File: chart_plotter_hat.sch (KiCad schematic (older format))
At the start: 41 parts, among them J1 Conn_01x06, J2 Conn_01x04, J3 40HAT, J4 Conn_01x04, J5 Conn_01x04, J6 Conn_01x02, J7 Conn_01x04, J8 Conn_02x03_Odd_Even, J9 Conn_01x03, Q1 DMG2305UX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

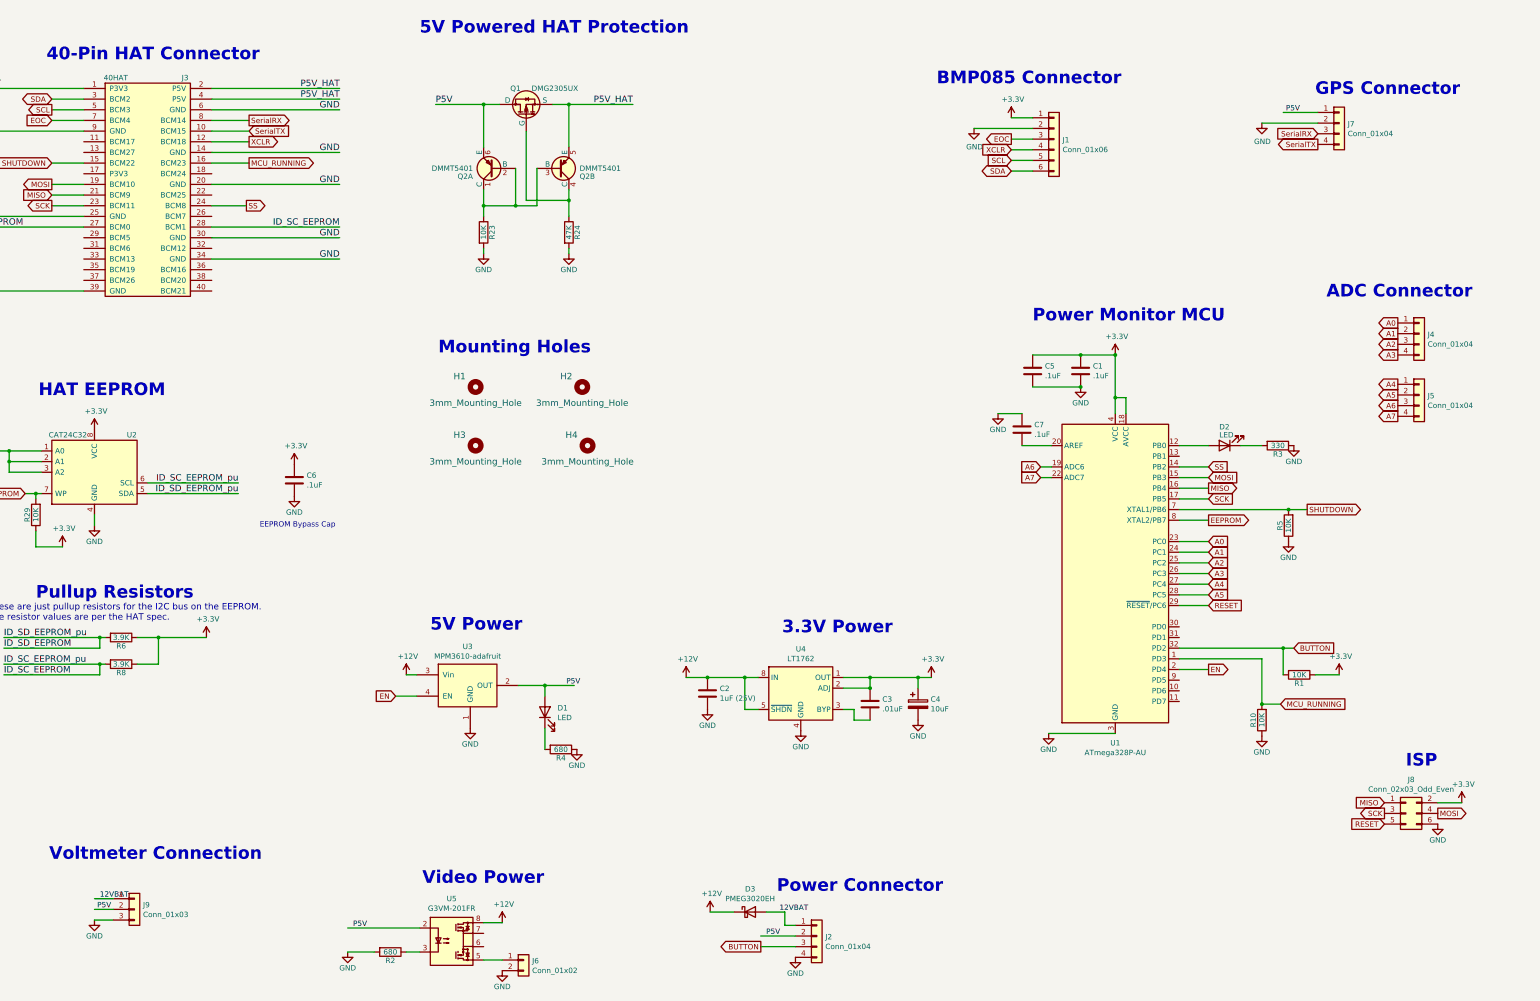
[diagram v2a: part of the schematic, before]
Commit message: Added Inductor to AVCC
Added optional 12VBAT adc on A7
Changed P5V label to +5V
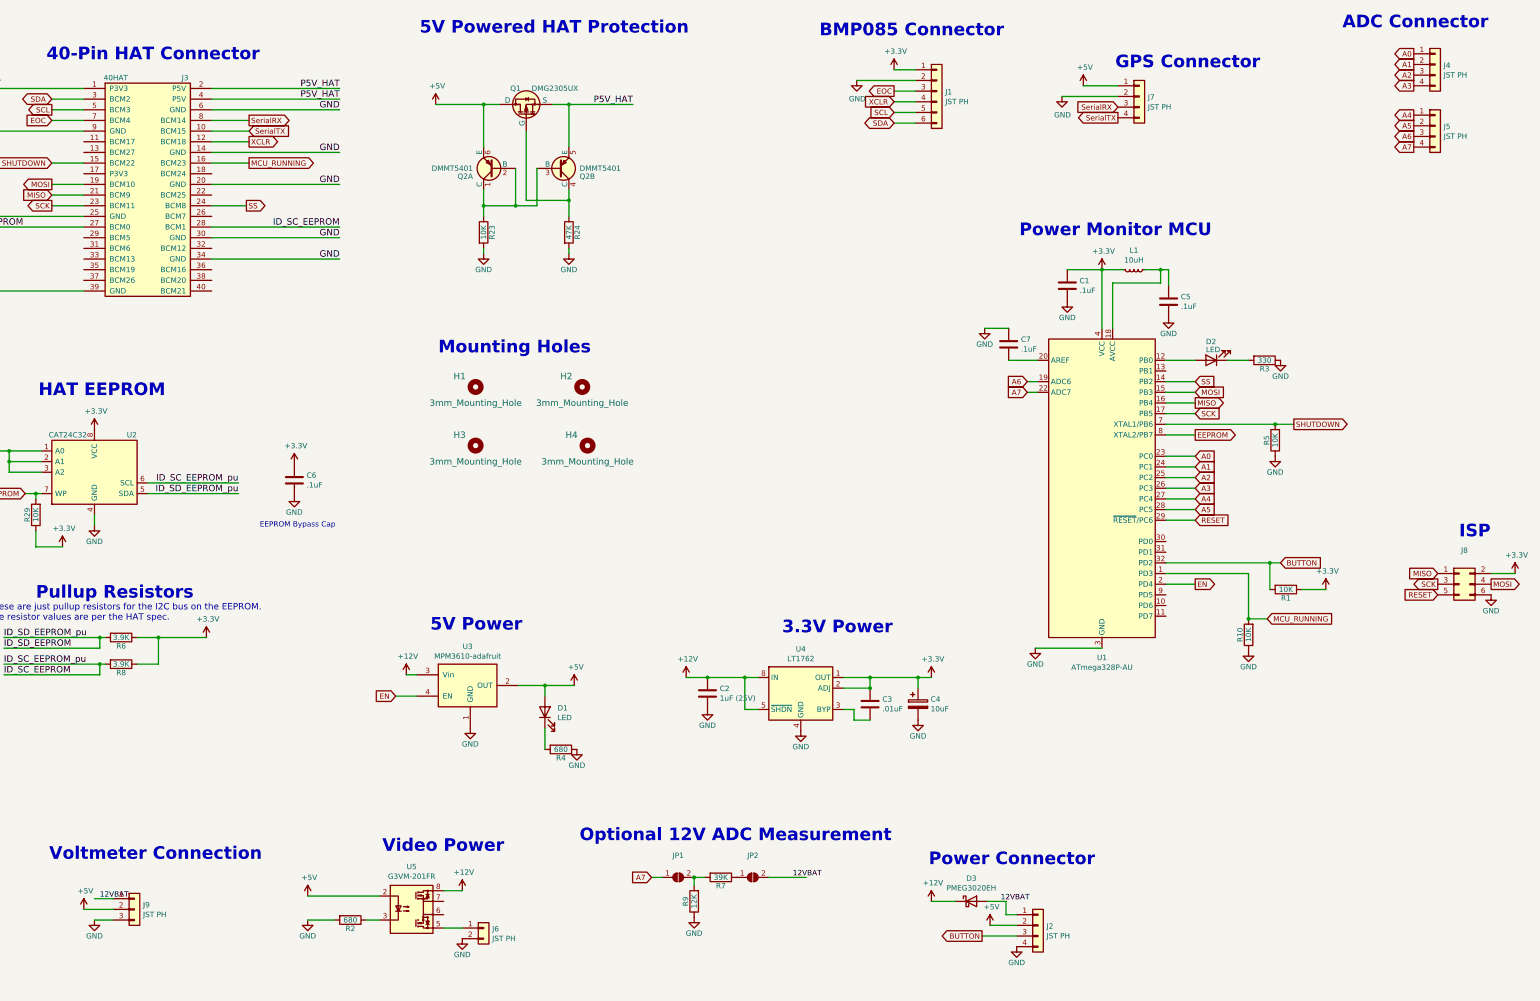
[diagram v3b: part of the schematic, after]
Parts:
- added JP1, JP2: SolderJumper_2_Open, CustomComponents:SolderJumper-2_P1.3mm_Open_RoundedPad1.0x1.5mm, symbol Jumper:SolderJumper_2_Open
- added L1: 10uH, Capacitors_SMD:C_0603, symbol Device:L_Small
- added R7: 39K, Resistors_SMD:R_0603, symbol Device:R
- added R9: 12K, Resistors_SMD:R_0603, symbol Device:R
- J1: value Conn_01x06 -> JST PH
- J2, J4, J5, J7: value Conn_01x04 -> JST PH
- J6: value Conn_01x02 -> JST PH
- J9: value Conn_01x03 -> JST PH
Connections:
- net labels added: +5V
- net labels removed: P5V
- wire segments 149 -> 155
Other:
- note added: "Optional 12V ADC Measurement"
- moved on the sheet: C1, C5, C7, D2, D3, J1, J2, J4, J5, J6, J7, J8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

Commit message: Added pdf of original release
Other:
- note added: "To use, solder both bridges, and populate R7 and R9"
- moved on the sheet: C1, C2, C3, C4, C5, C6, C7, D1, D2, D3, J2, J6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

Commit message: Moved CS to PD3, MCU_RUNNING to PB1
Renamed SS to CS
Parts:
- C2: value 1uF (25V) -> 1uF; Voltage (none) -> 25V
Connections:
- net MCU_RUNNING: now also U1.13 (PB1); no longer U1.1 (PD3)
- net SS: no longer names the net of U1.14 (PB2)
- net SS: no longer J3.24 (BCM8)
- new net CS: J3.24 (BCM8), U1.1 (PD3)
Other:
- moved on the sheet: R10
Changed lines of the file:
@@
 Wire Wire Line
 	13100 5925 13375 5925
-Text GLabel 13375 5625 2    50   Input ~ 0
-SS
-Wire Wire Line
-	13100 5625 13375 5625
+Text GLabel 13375 7425 2    50   Input ~ 0
+CS
+Wire Wire Line
+	13100 5525 14950 5525
 Wire Wire Line
 	13100 7525 13375 7525
@@
 	2000 3350 1700 3350
 Text GLabel 3525 3350 2    50   Output ~ 0
-SS
+CS
 Wire Wire Line
 	3200 3350 3525 3350
@@
 Text GLabel 14300 6025 2    50   Output ~ 0
 SHUTDOWN
-Text GLabel 14050 7850 2    50   Input ~ 0
+Text GLabel 15125 5950 2    50   Input ~ 0
 MCU_RUNNING
 Text GLabel 14175 7325 2    50   Input ~ 0
@@
 L power:GND #PWR015
 U 1 1 5FDCD1F3
-P 13875 8150
-F 0 "#PWR015" H 13875 7900 50  0001 C CNN
-F 1 "GND" H 13875 8000 50  0000 C CNN
-F 2 "" H 13875 8150 50  0000 C CNN
-F 3 "" H 13875 8150 50  0000 C CNN
-	1    13875 8150
+P 14950 6250
+F 0 "#PWR015" H 14950 6000 50  0001 C CNN
+F 1 "GND" H 14950 6100 50  0000 C CNN
+F 2 "" H 14950 6250 50  0000 C CNN
+F 3 "" H 14950 6250 50  0000 C CNN
+	1    14950 6250
 	1    0    0    -1
 $EndComp
@@
 P 7850 7525
 F 0 "C2" H 7965 7571 50  0000 L CNN
-F 1 "1uF (25V)" H 7965 7480 50  0000 L CNN
+F 1 "1uF" H 7965 7480 50  0000 L CNN
 F 2 "Capacitors_SMD:C_1206" H 7888 7375 50  0001 C CNN
 F 3 "~" H 7850 7525 50  0001 C CNN
+F 4 "25V" H 8025 7400 50  0000 C CNN "Voltage"
 	1    7850 7525
 	1    0    0    -1
@@
 	3200 2950 3550 2950
 Wire Wire Line
-	13875 7425 13875 7850
-Wire Wire Line
-	13875 7850 14050 7850
-Wire Wire Line
-	13100 7425 13875 7425
+	14950 5525 14950 5950
+Wire Wire Line
+	14950 5950 15125 5950
 $Comp
 L Device:R R10
 U 1 1 5FF805D9
-P 13875 8000
-F 0 "R10" V 13955 8000 50  0000 C CNN
-F 1 "10K" V 13875 8000 50  0000 C CNN
-F 2 "Resistors_SMD:R_0603" V 13805 8000 50  0001 C CNN
-F 3 "" H 13875 8000 50  0001 C CNN
-	1    13875 8000
+P 14950 6100
+F 0 "R10" V 15030 6100 50  0000 C CNN
+F 1 "10K" V 14950 6100 50  0000 C CNN
+F 2 "Resistors_SMD:R_0603" V 14880 6100 50  0001 C CNN
+F 3 "" H 14950 6100 50  0001 C CNN
+	1    14950 6100
 	-1   0    0    1
 $EndComp
-Connection ~ 13875 7850
+Connection ~ 14950 5950
 $Comp
 L power:GND #PWR0111
@@
 Text Notes 6575 9450 0    50   ~ 0
 To use, solder both bridges, and populate R7 and R9
+Wire Wire Line
+	13100 7425 13375 7425
 $EndSCHEMATC

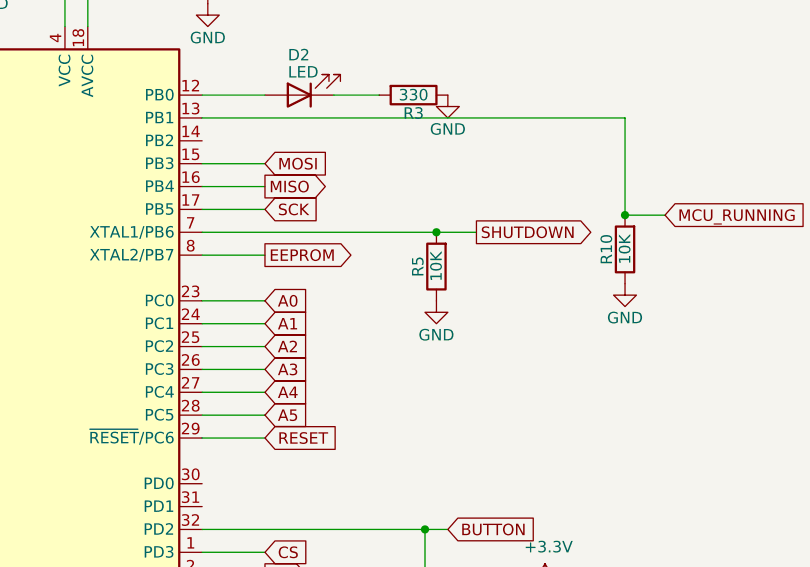
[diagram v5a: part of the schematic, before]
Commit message: Removed pull down on SHUTDOWN, not needed
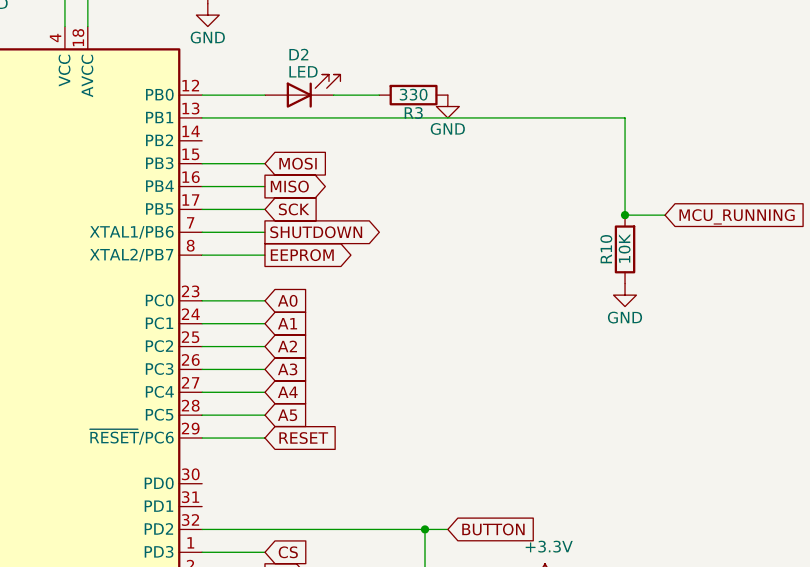
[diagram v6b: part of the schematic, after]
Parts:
- removed R5: 10K, Resistors_SMD:R_0603, symbol Device:R
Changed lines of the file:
@@
 	1    0    0    -1
 $EndComp
-Text GLabel 14300 6025 2    50   Output ~ 0
+Text GLabel 13375 6025 2    50   Output ~ 0
 SHUTDOWN
 Text GLabel 15125 5950 2    50   Input ~ 0
@@
 	13675 5425 13875 5425
 $Comp
-L Device:R R5
-U 1 1 6013CE2D
-P 14125 6175
-F 0 "R5" V 14205 6175 50  0000 C CNN
-F 1 "10K" V 14125 6175 50  0000 C CNN
-F 2 "Resistors_SMD:R_0603" V 14055 6175 50  0001 C CNN
-F 3 "" H 14125 6175 50  0001 C CNN
-	1    14125 6175
-	-1   0    0    1
-$EndComp
-Wire Wire Line
-	13100 6025 14125 6025
-Connection ~ 14125 6025
-Wire Wire Line
-	14125 6025 14300 6025
-$Comp
-L power:GND #PWR04
-U 1 1 6014DAF4
-P 14125 6325
-F 0 "#PWR04" H 14125 6075 50  0001 C CNN
-F 1 "GND" H 14125 6175 50  0000 C CNN
-F 2 "" H 14125 6325 50  0000 C CNN
-F 3 "" H 14125 6325 50  0000 C CNN
-	1    14125 6325
-	1    0    0    -1
-$EndComp
-$Comp
 L Diode:PMEG3020EH D3
 U 1 1 6019111C
@@
 Wire Wire Line
 	13100 7425 13375 7425
+Wire Wire Line
+	13100 6025 13375 6025
 $EndSCHEMATC

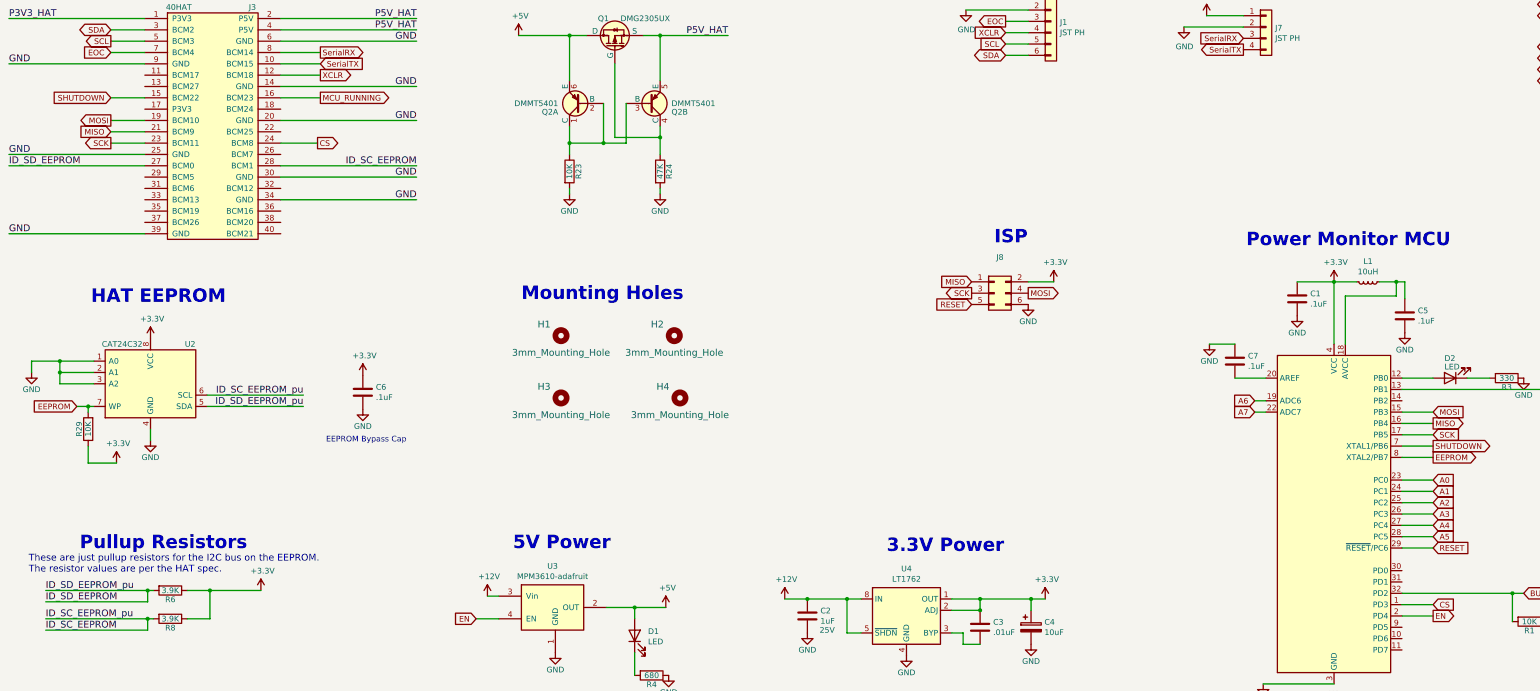
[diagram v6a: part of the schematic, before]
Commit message: Routed BUTTON to the Pi also
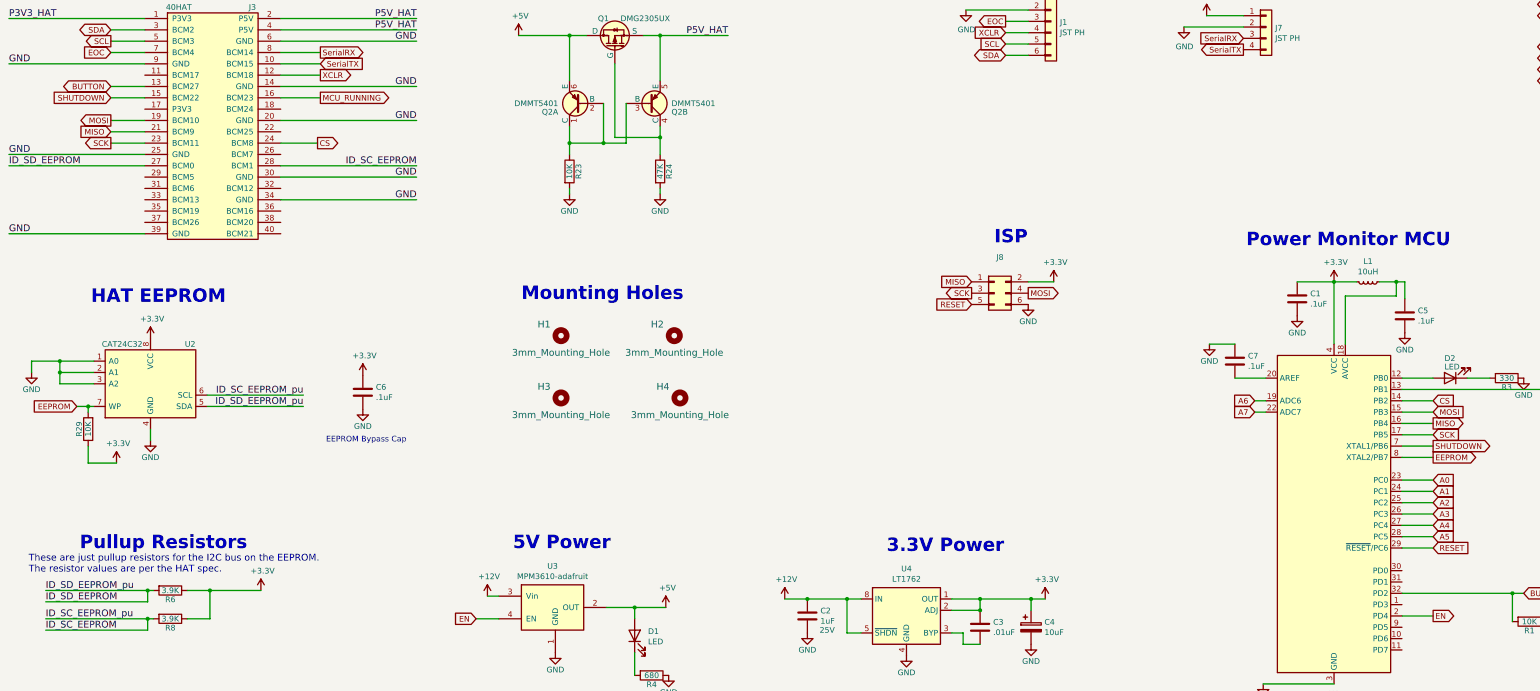
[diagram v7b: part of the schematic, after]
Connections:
- net BUTTON: now also J3.13 (BCM27)
- net CS: now also U1.14 (PB2); no longer U1.1 (PD3)
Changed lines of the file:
@@
 Wire Wire Line
 	13100 5925 13375 5925
-Text GLabel 13375 7425 2    50   Input ~ 0
+Text GLabel 13375 5625 2    50   Input ~ 0
 CS
 Wire Wire Line
@@
 To use, solder both bridges, and populate R7 and R9
 Wire Wire Line
-	13100 7425 13375 7425
-Wire Wire Line
 	13100 6025 13375 6025
+Wire Wire Line
+	13100 5625 13375 5625
+Text GLabel 1700 2850 0    50   BiDi ~ 0
+BUTTON
+Wire Wire Line
+	1700 2850 2000 2850
 $EndSCHEMATC
